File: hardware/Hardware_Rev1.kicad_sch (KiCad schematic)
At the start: 52 parts, among them J1 RJ45_LED_Shielded, J2 6P6C, Q1 BUK7M33-60EX, Q2 BUK7M33-60EX, Q3 BUK7M33-60EX, U1 LT1910, U2 LT1910, U3 OKI, U4 LT1910, U5 TSR_1-2450, U6 Teensy4.1_DEV-16771

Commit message: Finished Schematic, kinda finished BOM, layout tomorrow.
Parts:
- D1: value LED -> LED(G)
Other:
- note added: "Andersons"
- note added: "Bucks"
- note added: "Drive Circuit(s)"
- note added: "Duh Teensy"
- company: James Elverson, Katie McNevin, Joshua Perkins -> Jacob Byers(?), James Elverson, Joshua Perkins
- moved on the sheet: C3, C6, C7, Conn1C, D1, D4, D5, R3, R6, R8, U5

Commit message: Started Layout + Added Vias
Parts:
- added V? (x4): Via, symbol MRDT_Drill_Holes:Via
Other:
- company: Jacob Byers(?), James Elverson, Joshua Perkins -> Jacob Byers, James Elverson, Joshua Perkins
- title: Science Heater Board - Rev1 -> Water Heater Board - Rev1
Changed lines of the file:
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@@
   (paper "A4")
   (title_block
-    (title "Science Heater Board - Rev1")
+    (title "Water Heater Board - Rev1")
     (rev "1")
-    (company "Jacob Byers(?), James Elverson, Joshua Perkins")
+    (company "Jacob Byers, James Elverson, Joshua Perkins")
     (comment 4 "MRDT")
   )
@@
     (property "Datasheet" "" (id 3) (at 30.48 38.1 0)
       (effects (font (size 1.27 1.27)) hide)
+    )
+    (pin "1")
+  )
+  (symbol (lib_id "MRDT_Drill_Holes:Via") (at 152.4 124.46 0) (unit 1)
+    (in_bom yes) (on_board yes) (fields_autoplaced)
+    (property "Reference" "V?" (id 0) (at 158.75 123.19 0)
+      (effects (font (size 1.524 1.524)) (justify left))
+    )
+    (property "Value" "Via" (id 1) (at 158.75 127 0)
+      (effects (font (size 1.524 1.524)) (justify left))
+    )
+    (property "Footprint" "" (id 2) (at 152.4 124.46 0)
+      (effects (font (size 1.524 1.524)) hide)
+    )
+    (property "Datasheet" "" (id 3) (at 152.4 124.46 0)
+      (effects (font (size 1.524 1.524)) hide)
     )
     (pin "1")
@@
     (pin "1")
   )
+  (symbol (lib_id "MRDT_Drill_Holes:Via") (at 152.4 118.11 0) (unit 1)
+    (in_bom yes) (on_board yes) (fields_autoplaced)
+    (property "Reference" "V?" (id 0) (at 158.75 116.84 0)
+      (effects (font (size 1.524 1.524)) (justify left))
+    )
+    (property "Value" "Via" (id 1) (at 158.75 120.65 0)
+      (effects (font (size 1.524 1.524)) (justify left))
+    )
+    (property "Footprint" "" (id 2) (at 152.4 118.11 0)
+      (effects (font (size 1.524 1.524)) hide)
+    )
+    (property "Datasheet" "" (id 3) (at 152.4 118.11 0)
+      (effects (font (size 1.524 1.524)) hide)
+    )
+    (pin "1")
+  )
   (symbol (lib_id "power:GND") (at 139.7 33.655 0) (unit 1)
     (in_bom yes) (on_board yes) (fields_autoplaced)
@@
     (pin "1")
   )
+  (symbol (lib_id "MRDT_Drill_Holes:Via") (at 158.75 130.81 0) (unit 1)
+    (in_bom yes) (on_board yes) (fields_autoplaced)
+    (property "Reference" "V?" (id 0) (at 165.1 129.54 0)
+      (effects (font (size 1.524 1.524)) (justify left))
+    )
+    (property "Value" "Via" (id 1) (at 165.1 133.35 0)
+      (effects (font (size 1.524 1.524)) (justify left))
+    )
+    (property "Footprint" "" (id 2) (at 158.75 130.81 0)
+      (effects (font (size 1.524 1.524)) hide)
+    )
+    (property "Datasheet" "" (id 3) (at 158.75 130.81 0)
+      (effects (font (size 1.524 1.524)) hide)
+    )
+    (pin "1")
+  )
   (symbol (lib_id "Device:R") (at 75.565 92.71 0) (unit 1)
     (in_bom yes) (on_board yes)
@@
     (pin "1")
   )
+  (symbol (lib_id "MRDT_Drill_Holes:Via") (at 152.4 130.81 0) (unit 1)
+    (in_bom yes) (on_board yes) (fields_autoplaced)
+    (property "Reference" "V?" (id 0) (at 158.75 129.54 0)
+      (effects (font (size 1.524 1.524)) (justify left))
+    )
+    (property "Value" "Via" (id 1) (at 158.75 133.35 0)
+      (effects (font (size 1.524 1.524)) (justify left))
+    )
+    (property "Footprint" "" (id 2) (at 152.4 130.81 0)
+      (effects (font (size 1.524 1.524)) hide)
+    )
+    (property "Datasheet" "" (id 3) (at 152.4 130.81 0)
+      (effects (font (size 1.524 1.524)) hide)
+    )
+    (pin "1")
+  )
   (symbol (lib_id "Device:LED") (at 198.755 59.69 0) (unit 1)
     (in_bom yes) (on_board yes)
@@
       (reference "U6") (unit 1) (value "Teensy4.1_DEV-16771") (footprint "MRDT_Shields:Teensy_4_1_Vertical")
     )
-  )
+    (path "/03f6edf9-5a1f-44e9-b14d-667e1c68bccb"
+      (reference "V?") (unit 1) (value "Via") (footprint "")
+    )
+    (path "/8053e13e-7718-49bc-b6d0-eac399e3fb77"
+      (reference "V?") (unit 1) (value "Via") (footprint "")
+    )
+    (path "/dd283265-6848-445d-b403-1b7af06bee49"
+      (reference "V?") (unit 1) (value "Via") (footprint "")
+    )
+    (path "/f1caf4e7-92af-4314-9bd9-309c36aa8573"
+      (reference "V?") (unit 1) (value "Via") (footprint "")
+    )
+  )

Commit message: mmm mosfets are good now!
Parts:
- Q1, Q2, Q3: value BUK7M33-60EX -> BUK9M9R5-40HX
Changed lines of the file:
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@@
       (effects (font (size 1.27 1.27)) (justify left))
     )
-    (property "Value" "BUK7M33-60EX" (id 1) (at 141.859 74.295 0)
-      (effects (font (size 1.27 1.27)) (justify left))
+    (property "Value" "BUK9M9R5-40HX" (id 1) (at 141.859 74.295 0)
+      (effects (font (size 1.24 1.24)) (justify left))
     )
     (property "Footprint" "Package_TO_SOT_SMD:LFPAK33" (id 2) (at 160.909 81.28 0)
@@
       (effects (font (size 1.27 1.27)) (justify left))
     )
-    (property "Value" "BUK7M33-60EX" (id 1) (at 58.42 130.175 0)
-      (effects (font (size 1.27 1.27)) (justify left))
+    (property "Value" "BUK9M9R5-40HX" (id 1) (at 58.42 130.175 0)
+      (effects (font (size 1.24 1.24)) (justify left))
     )
     (property "Footprint" "Package_TO_SOT_SMD:LFPAK33" (id 2) (at 77.47 137.16 0)
@@
       (effects (font (size 1.27 1.27)) (justify left))
     )
-    (property "Value" "BUK7M33-60EX" (id 1) (at 59.055 77.47 0)
-      (effects (font (size 1.27 1.27)) (justify left))
+    (property "Value" "BUK9M9R5-40HX" (id 1) (at 59.055 77.47 0)
+      (effects (font (size 1.24 1.24)) (justify left))
     )
     (property "Footprint" "Package_TO_SOT_SMD:LFPAK33" (id 2) (at 78.105 84.455 0)
@@
     )
     (path "/5435883c-e392-4c8a-a401-8713ea7726de"
-      (reference "Q1") (unit 1) (value "BUK7M33-60EX") (footprint "Package_TO_SOT_SMD:LFPAK33")
+      (reference "Q1") (unit 1) (value "BUK9M9R5-40HX") (footprint "Package_TO_SOT_SMD:LFPAK33")
     )
     (path "/9bcb1452-d9a0-4902-bc18-7e17d1c3d39d"
-      (reference "Q2") (unit 1) (value "BUK7M33-60EX") (footprint "Package_TO_SOT_SMD:LFPAK33")
+      (reference "Q2") (unit 1) (value "BUK9M9R5-40HX") (footprint "Package_TO_SOT_SMD:LFPAK33")
     )
     (path "/292ead5a-18b0-4c0f-98c8-834c840b4e1c"
-      (reference "Q3") (unit 1) (value "BUK7M33-60EX") (footprint "Package_TO_SOT_SMD:LFPAK33")
+      (reference "Q3") (unit 1) (value "BUK9M9R5-40HX") (footprint "Package_TO_SOT_SMD:LFPAK33")
     )
     (path "/e97810e0-a79e-4627-b896-aa8f7aca4bf4"

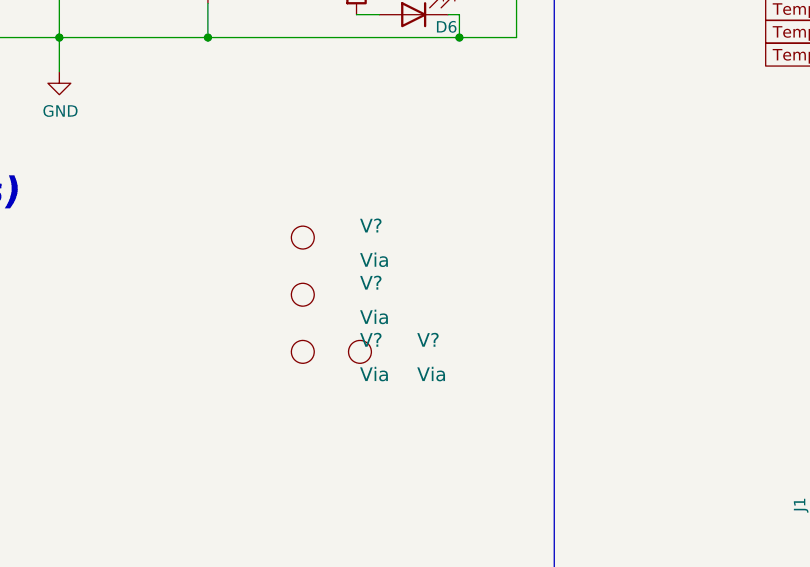
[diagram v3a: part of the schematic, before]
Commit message: updated layout with drill holes (they don't fit??)
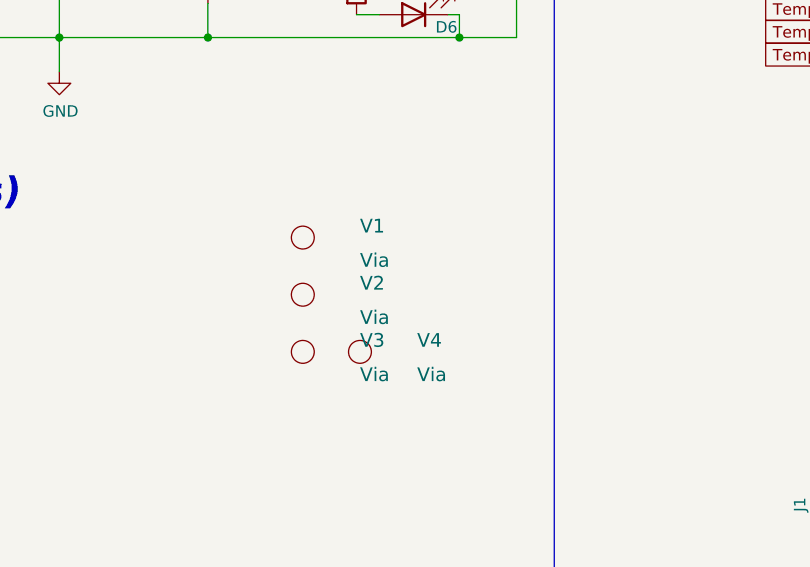
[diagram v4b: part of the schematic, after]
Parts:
- V1, V2, V3, V4: renamed from V?; footprint (none) -> MRDT_Drill_Holes:4_40_Hole_Corner
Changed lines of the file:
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@@
   (symbol (lib_id "MRDT_Drill_Holes:Via") (at 152.4 124.46 0) (unit 1)
     (in_bom yes) (on_board yes) (fields_autoplaced)
-    (property "Reference" "V?" (id 0) (at 158.75 123.19 0)
+    (property "Reference" "V2" (id 0) (at 158.75 123.19 0)
       (effects (font (size 1.524 1.524)) (justify left))
     )
@@
       (effects (font (size 1.524 1.524)) (justify left))
     )
-    (property "Footprint" "" (id 2) (at 152.4 124.46 0)
+    (property "Footprint" "MRDT_Drill_Holes:4_40_Hole_Corner" (id 2) (at 152.4 124.46 0)
       (effects (font (size 1.524 1.524)) hide)
     )
@@
   (symbol (lib_id "MRDT_Drill_Holes:Via") (at 152.4 118.11 0) (unit 1)
     (in_bom yes) (on_board yes) (fields_autoplaced)
-    (property "Reference" "V?" (id 0) (at 158.75 116.84 0)
+    (property "Reference" "V1" (id 0) (at 158.75 116.84 0)
       (effects (font (size 1.524 1.524)) (justify left))
     )
@@
       (effects (font (size 1.524 1.524)) (justify left))
     )
-    (property "Footprint" "" (id 2) (at 152.4 118.11 0)
+    (property "Footprint" "MRDT_Drill_Holes:4_40_Hole_Corner" (id 2) (at 152.4 118.11 0)
       (effects (font (size 1.524 1.524)) hide)
     )
@@
   (symbol (lib_id "MRDT_Drill_Holes:Via") (at 158.75 130.81 0) (unit 1)
     (in_bom yes) (on_board yes) (fields_autoplaced)
-    (property "Reference" "V?" (id 0) (at 165.1 129.54 0)
+    (property "Reference" "V4" (id 0) (at 165.1 129.54 0)
       (effects (font (size 1.524 1.524)) (justify left))
     )
@@
       (effects (font (size 1.524 1.524)) (justify left))
     )
-    (property "Footprint" "" (id 2) (at 158.75 130.81 0)
+    (property "Footprint" "MRDT_Drill_Holes:4_40_Hole_Corner" (id 2) (at 158.75 130.81 0)
       (effects (font (size 1.524 1.524)) hide)
     )
@@
   (symbol (lib_id "MRDT_Drill_Holes:Via") (at 152.4 130.81 0) (unit 1)
     (in_bom yes) (on_board yes) (fields_autoplaced)
-    (property "Reference" "V?" (id 0) (at 158.75 129.54 0)
+    (property "Reference" "V3" (id 0) (at 158.75 129.54 0)
       (effects (font (size 1.524 1.524)) (justify left))
     )
@@
       (effects (font (size 1.524 1.524)) (justify left))
     )
-    (property "Footprint" "" (id 2) (at 152.4 130.81 0)
+    (property "Footprint" "MRDT_Drill_Holes:4_40_Hole_Corner" (id 2) (at 152.4 130.81 0)
       (effects (font (size 1.524 1.524)) hide)
     )
@@
       (reference "U6") (unit 1) (value "Teensy4.1_DEV-16771") (footprint "MRDT_Shields:Teensy_4_1_Vertical")
     )
+    (path "/8053e13e-7718-49bc-b6d0-eac399e3fb77"
+      (reference "V1") (unit 1) (value "Via") (footprint "MRDT_Drill_Holes:4_40_Hole_Corner")
+    )
     (path "/03f6edf9-5a1f-44e9-b14d-667e1c68bccb"
-      (reference "V?") (unit 1) (value "Via") (footprint "")
-    )
-    (path "/8053e13e-7718-49bc-b6d0-eac399e3fb77"
-      (reference "V?") (unit 1) (value "Via") (footprint "")
+      (reference "V2") (unit 1) (value "Via") (footprint "MRDT_Drill_Holes:4_40_Hole_Corner")
+    )
+    (path "/f1caf4e7-92af-4314-9bd9-309c36aa8573"
+      (reference "V3") (unit 1) (value "Via") (footprint "MRDT_Drill_Holes:4_40_Hole_Corner")
     )
     (path "/dd283265-6848-445d-b403-1b7af06bee49"
-      (reference "V?") (unit 1) (value "Via") (footprint "")
-    )
-    (path "/f1caf4e7-92af-4314-9bd9-309c36aa8573"
-      (reference "V?") (unit 1) (value "Via") (footprint "")
-    )
-  )
+      (reference "V4") (unit 1) (value "Via") (footprint "MRDT_Drill_Holes:4_40_Hole_Corner")
+    )
+  )

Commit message: other
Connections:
- net +12VA is gone; now on net +12V: C10.1, C4.1, C5.1, Conn1.3 (V+Act), Q1.5 (D), Q2.5 (D), Q3.5 (D), R3.1, U1.6 (SENSE), U1.8 (V+), U2.6 (SENSE), U2.8 (V+), U4.6 (SENSE), U4.8 (V+)
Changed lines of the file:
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@@
     (pin "2")
-  )
-  (symbol (lib_id "power:+12VA") (at 30.48 38.1 0) (unit 1)
-    (in_bom yes) (on_board yes) (fields_autoplaced)
-    (property "Reference" "#PWR0103" (id 0) (at 30.48 41.91 0)
-      (effects (font (size 1.27 1.27)) hide)
-    )
-    (property "Value" "+12VA" (id 1) (at 30.48 33.02 0))
-    (property "Footprint" "" (id 2) (at 30.48 38.1 0)
-      (effects (font (size 1.27 1.27)) hide)
-    )
-    (property "Datasheet" "" (id 3) (at 30.48 38.1 0)
-      (effects (font (size 1.27 1.27)) hide)
-    )
-    (pin "1")
   )
   (symbol (lib_id "MRDT_Drill_Holes:Via") (at 152.4 124.46 0) (unit 1)
@@
     (pin "2")
   )
-  (symbol (lib_id "power:+12VA") (at 58.42 122.555 0) (unit 1)
-    (in_bom yes) (on_board yes)
-    (property "Reference" "#PWR0117" (id 0) (at 58.42 126.365 0)
-      (effects (font (size 1.27 1.27)) hide)
-    )
-    (property "Value" "+12VA" (id 1) (at 58.801 118.1608 0))
-    (property "Footprint" "" (id 2) (at 58.42 122.555 0)
-      (effects (font (size 1.27 1.27)) hide)
-    )
-    (property "Datasheet" "" (id 3) (at 58.42 122.555 0)
-      (effects (font (size 1.27 1.27)) hide)
-    )
-    (pin "1")
-  )
-  (symbol (lib_id "power:+12VA") (at 59.055 69.85 0) (unit 1)
-    (in_bom yes) (on_board yes)
-    (property "Reference" "#PWR0109" (id 0) (at 59.055 73.66 0)
-      (effects (font (size 1.27 1.27)) hide)
-    )
-    (property "Value" "+12VA" (id 1) (at 59.436 65.4558 0))
-    (property "Footprint" "" (id 2) (at 59.055 69.85 0)
-      (effects (font (size 1.27 1.27)) hide)
-    )
-    (property "Datasheet" "" (id 3) (at 59.055 69.85 0)
-      (effects (font (size 1.27 1.27)) hide)
-    )
-    (pin "1")
-  )
   (symbol (lib_id "power:+5V") (at 17.145 69.85 0) (unit 1)
     (in_bom yes) (on_board yes)
@@
     (pin "1")
   )
+  (symbol (lib_id "power:+12V") (at 141.859 66.675 0) (unit 1)
+    (in_bom yes) (on_board yes) (fields_autoplaced)
+    (property "Reference" "#PWR?" (id 0) (at 141.859 70.485 0)
+      (effects (font (size 1.27 1.27)) hide)
+    )
+    (property "Value" "+12V" (id 1) (at 141.859 61.595 0))
+    (property "Footprint" "" (id 2) (at 141.859 66.675 0)
+      (effects (font (size 1.27 1.27)) hide)
+    )
+    (property "Datasheet" "" (id 3) (at 141.859 66.675 0)
+      (effects (font (size 1.27 1.27)) hide)
+    )
+    (pin "1")
+  )
   (symbol (lib_id "MRDT_Connectors:Molex_uF_S_03") (at 147.574 63.5 270) (unit 1)
     (in_bom yes) (on_board yes)
@@
     )
     (property "Datasheet" "" (id 3) (at 188.595 54.61 0)
+      (effects (font (size 1.27 1.27)) hide)
+    )
+    (pin "1")
+  )
+  (symbol (lib_id "power:+12V") (at 58.42 122.555 0) (unit 1)
+    (in_bom yes) (on_board yes) (fields_autoplaced)
+    (property "Reference" "#PWR?" (id 0) (at 58.42 126.365 0)
+      (effects (font (size 1.27 1.27)) hide)
+    )
+    (property "Value" "+12V" (id 1) (at 58.42 117.475 0))
+    (property "Footprint" "" (id 2) (at 58.42 122.555 0)
+      (effects (font (size 1.27 1.27)) hide)
+    )
+    (property "Datasheet" "" (id 3) (at 58.42 122.555 0)
       (effects (font (size 1.27 1.27)) hide)
     )
@@
     (pin "1")
   )
-  (symbol (lib_id "power:+12VA") (at 141.859 66.675 0) (unit 1)
-    (in_bom yes) (on_board yes)
-    (property "Reference" "#PWR0114" (id 0) (at 141.859 70.485 0)
-      (effects (font (size 1.27 1.27)) hide)
-    )
-    (property "Value" "+12VA" (id 1) (at 142.24 62.2808 0))
-    (property "Footprint" "" (id 2) (at 141.859 66.675 0)
-      (effects (font (size 1.27 1.27)) hide)
-    )
-    (property "Datasheet" "" (id 3) (at 141.859 66.675 0)
-      (effects (font (size 1.27 1.27)) hide)
-    )
-    (pin "1")
-  )
   (symbol (lib_id "hardware-rescue:CP1-Device") (at 141.859 88.265 0) (unit 1)
     (in_bom yes) (on_board yes)
@@
     (pin "1")
     (pin "2")
+  )
+  (symbol (lib_id "power:+12V") (at 59.055 69.85 0) (unit 1)
+    (in_bom yes) (on_board yes) (fields_autoplaced)
+    (property "Reference" "#PWR?" (id 0) (at 59.055 73.66 0)
+      (effects (font (size 1.27 1.27)) hide)
+    )
+    (property "Value" "+12V" (id 1) (at 59.055 64.77 0))
+    (property "Footprint" "" (id 2) (at 59.055 69.85 0)
+      (effects (font (size 1.27 1.27)) hide)
+    )
+    (property "Datasheet" "" (id 3) (at 59.055 69.85 0)
+      (effects (font (size 1.27 1.27)) hide)
+    )
+    (pin "1")
   )
   (symbol (lib_id "Connector:RJ45_LED_Shielded") (at 222.885 146.05 0) (unit 1)
@@
     (pin "2")
   )
+  (symbol (lib_id "power:+12V") (at 30.48 38.1 0) (unit 1)
+    (in_bom yes) (on_board yes) (fields_autoplaced)
+    (property "Reference" "#PWR?" (id 0) (at 30.48 41.91 0)
+      (effects (font (size 1.27 1.27)) hide)
+    )
+    (property "Value" "+12V" (id 1) (at 30.48 33.02 0))
+    (property "Footprint" "" (id 2) (at 30.48 38.1 0)
+      (effects (font (size 1.27 1.27)) hide)
+    )
+    (property "Datasheet" "" (id 3) (at 30.48 38.1 0)
+      (effects (font (size 1.27 1.27)) hide)
+    )
+    (pin "1")
+  )
   (symbol (lib_id "power:GND") (at 41.91 155.575 0) (unit 1)
     (in_bom yes) (on_board yes)
@@
       (reference "#PWR0102") (unit 1) (value "+12V") (footprint "")
     )
-    (path "/035dce19-916d-4957-a323-9f119d307792"
-      (reference "#PWR0103") (unit 1) (value "+12VA") (footprint "")
-    )
     (path "/75394c0e-8deb-4c1b-96d9-90a95f192003"
       (reference "#PWR0104") (unit 1) (value "GND") (footprint "")
@@
       (reference "#PWR0108") (unit 1) (value "GND") (footprint "")
     )
-    (path "/3263b976-aa0b-4949-8702-e6a7d2e44e3f"
-      (reference "#PWR0109") (unit 1) (value "+12VA") (footprint "")
-    )
     (path "/63c3fe76-6fde-4d6c-afb2-01ec61b588d5"
       (reference "#PWR0110") (unit 1) (value "GND") (footprint "")
@@
       (reference "#PWR0113") (unit 1) (value "+5V") (footprint "")
     )
-    (path "/93650ca5-7aed-46ea-b36b-d9ae620733a3"
-      (reference "#PWR0114") (unit 1) (value "+12VA") (footprint "")
-    )
     (path "/922f24c8-466f-41c5-8127-0f6ae63baf77"
       (reference "#PWR0115") (unit 1) (value "+3V3") (footprint "")
@@
       (reference "#PWR0116") (unit 1) (value "GND") (footprint "")
     )
-    (path "/30b170f1-9335-400f-b4f7-8c90895ed04d"
-      (reference "#PWR0117") (unit 1) (value "+12VA") (footprint "")
-    )
     (path "/04c6b71a-cafe-45ba-93a8-bd4006176f79"
       (reference "#PWR0118") (unit 1) (value "+5V") (footprint "")
@@
       (reference "#PWR0128") (unit 1) (value "+3V3") (footprint "")
     )
+    (path "/48cce387-c736-4901-85b6-daf02546325a"
+      (reference "#PWR?") (unit 1) (value "+12V") (footprint "")
+    )
+    (path "/7e8f0dd8-d57d-485e-829d-61d442d4dabd"
+      (reference "#PWR?") (unit 1) (value "+12V") (footprint "")
+    )
+    (path "/bb8912d6-4d7c-4d26-9ef4-da2bad352ebb"
+      (reference "#PWR?") (unit 1) (value "+12V") (footprint "")
+    )
+    (path "/e56c2889-0dbe-4802-89f7-860e8514a767"
+      (reference "#PWR?") (unit 1) (value "+12V") (footprint "")
+    )
     (path "/242933d4-3a6b-43a6-accd-20cece429af3"

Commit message: the start of pain
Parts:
- removed C1, C8: 0.1uF, Capacitor_SMD:C_0603_1608Metric_Pad1.08x0.95mm_HandSolder, symbol Device:C
- removed C10, C4: 10uF 50V, Capacitor_SMD:C_0603_1608Metric_Pad1.08x0.95mm_HandSolder, symbol hardware-rescue:CP1-Device
- removed Conn10, Conn4, Conn5, Conn9: Molex_uF_S_02, MRDT_Connectors:MOLEX_uF_S_02_Horizontal, symbol MRDT_Connectors:Molex_uF_S_02
- removed Conn2, Conn8: Molex_uF_S_03, MRDT_Connectors:MOLEX_uF_S_03_Horizontal, symbol MRDT_Connectors:Molex_uF_S_03
- removed D2, D6: LED(B), LED_SMD:LED_0603_1608Metric_Pad1.05x0.95mm_HandSolder, symbol Device:LED
- removed Q1, Q3: BUK9M9R5-40HX, Package_TO_SOT_SMD:LFPAK33, symbol Transistor_FET:BUK7M33-60EX
- removed R1, R7: 5.1k, Resistor_SMD:R_0603_1608Metric_Pad0.98x0.95mm_HandSolder, symbol Device:R
- removed R4, R9: 1000, Resistor_SMD:R_0603_1608Metric_Pad0.98x0.95mm_HandSolder, symbol Device:R
- removed U1, U4: LT1910, Package_SO:SOIC-8-N7_3.9x4.9mm_P1.27mm, symbol MRDT_ICs:LT1910
- added D?: LED(B), LED_SMD:LED_0603_1608Metric_Pad1.05x0.95mm_HandSolder, symbol Device:LED
- added F?: Fuse, symbol Device:Fuse
- added Q?: IRF7606PBF, Package_SO:MSOP-8_3x3mm_P0.65mm, symbol Transistor_FET:IRF7606PBF
- added Q?: BSS138, Package_TO_SOT_SMD:SOT-23, symbol Transistor_FET:BSS138
- added R? (x3): R, symbol Device:R
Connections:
- new net: Q?.1 (S), Q?.2 (S), Q?.3 (S)
- new net: Q?.5 (D), Q?.6 (D), Q?.7 (D), Q?.8 (D)
